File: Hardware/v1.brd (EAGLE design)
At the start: 50 x 40 mm, 79 parts, among them IC1 LM324D, IC2 m328p, IC3 REG1117, J1 22-27-2061-06, J2 22-27-2021-02, J3 22-27-2021-02, J4 22-27-2031-03, J5 22-27-2041-04, Q1 BSS123, Q2 BSS123, Q3 BSS123, Q5 BSS123

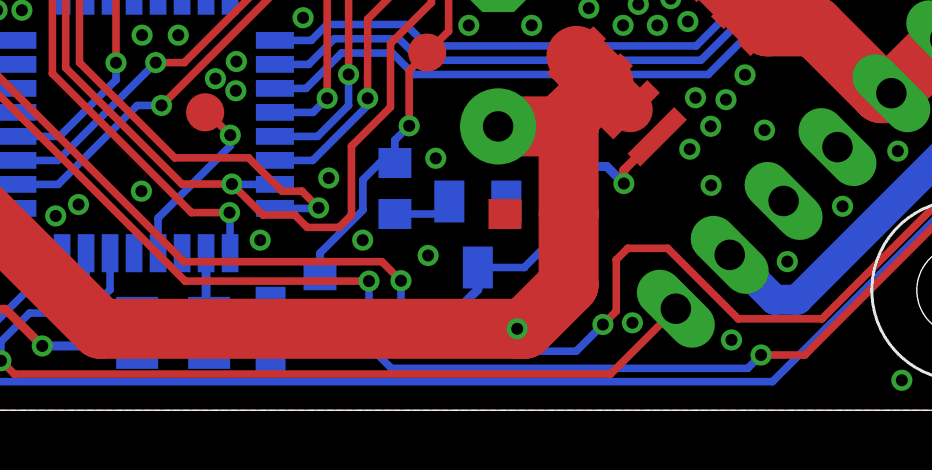
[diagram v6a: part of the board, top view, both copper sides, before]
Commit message: some ground issues fixed
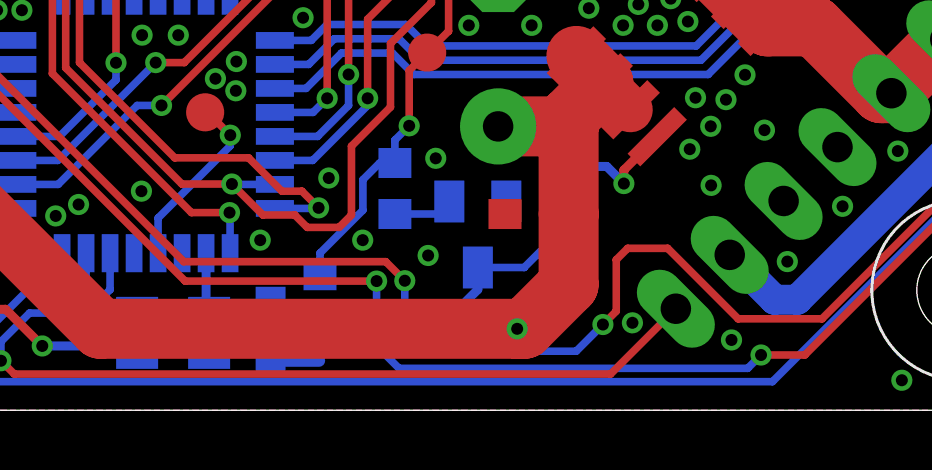
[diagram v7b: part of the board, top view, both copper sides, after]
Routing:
- net GND: track 7.48 -> 9.18 mm
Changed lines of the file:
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@@
 <wire x1="22.098" y1="39.116" x2="22.098" y2="38.13175" width="0.3" layer="16"/>
 <wire x1="22.098" y1="38.13175" x2="22.09165" y2="38.1254" width="0.3" layer="16"/>
-<wire x1="24.60625" y1="2.80125" x2="22.958425" y2="1.864625" width="0" layer="19" extent="16-16"/>
-<wire x1="26.02865" y1="5.67055" x2="24.60625" y2="2.80125" width="0" layer="19" extent="16-16"/>
+<wire x1="22.958425" y1="1.864625" x2="23.17205" y2="1.651" width="0.4064" layer="16"/>
+<wire x1="23.17205" y1="1.651" x2="24.5745" y2="1.651" width="0.4064" layer="16"/>
 </signal>
 <signal name="N$1">
@@
 <wire x1="48.26" y1="12.192" x2="48.26" y2="9.3345" width="0.254" layer="1"/>
 <wire x1="48.26" y1="9.3345" x2="40.767" y2="1.8415" width="0.254" layer="1"/>
-<wire x1="38.862" y1="1.397" x2="26.9875" y2="1.397" width="0.254" layer="16"/>
-<wire x1="26.9875" y1="1.397" x2="26.2382" y2="2.1463" width="0.254" layer="16"/>
-<via x="26.2382" y="4.3053" extent="1-16" drill="0.4"/>
+<wire x1="38.862" y1="1.397" x2="27.2415" y2="1.397" width="0.254" layer="16"/>
+<wire x1="27.2415" y1="1.397" x2="26.4922" y2="2.1463" width="0.254" layer="16"/>
+<via x="26.4922" y="4.3053" extent="1-16" drill="0.4"/>
 <wire x1="38.862" y1="1.397" x2="39.3065" y2="1.8415" width="0.254" layer="16"/>
 <via x="39.3065" y="1.8415" extent="1-16" drill="0.4"/>
-<wire x1="26.2382" y1="4.3053" x2="20.11045" y2="4.3053" width="0.254" layer="1"/>
+<wire x1="26.4922" y1="4.3053" x2="20.11045" y2="4.3053" width="0.254" layer="1"/>
 <wire x1="20.11045" y1="4.3053" x2="12.5095" y2="11.90625" width="0.254" layer="1"/>
 <wire x1="12.5095" y1="11.90625" x2="12.09675" y2="11.90625" width="0.254" layer="1"/>
 <wire x1="39.3065" y1="1.8415" x2="40.767" y2="1.8415" width="0.254" layer="1"/>
-<wire x1="26.2382" y1="2.1463" x2="26.2382" y2="4.3053" width="0.254" layer="16"/>
+<wire x1="26.4922" y1="2.1463" x2="26.4922" y2="4.3053" width="0.254" layer="16"/>
 </signal>
 <signal name="BUTTON_-">
@@
 <wire x1="34.8615" y1="5.3975" x2="34.4805" y2="5.0165" width="0.254" layer="1"/>
 <wire x1="34.4805" y1="5.0165" x2="34.4805" y2="3.302" width="0.254" layer="1"/>
-<via x="27.305" y="4.318" extent="1-16" drill="0.4"/>
-<wire x1="27.305" y1="4.318" x2="27.305" y2="2.413" width="0.254" layer="16"/>
-<wire x1="27.305" y1="2.413" x2="27.7495" y2="1.9685" width="0.254" layer="16"/>
-<wire x1="27.7495" y1="1.9685" x2="33.147" y2="1.9685" width="0.254" layer="16"/>
+<via x="27.432" y="4.318" extent="1-16" drill="0.4"/>
+<wire x1="27.432" y1="4.318" x2="27.432" y2="2.413" width="0.254" layer="16"/>
+<wire x1="27.432" y1="2.413" x2="27.8765" y2="1.9685" width="0.254" layer="16"/>
+<wire x1="27.8765" y1="1.9685" x2="33.147" y2="1.9685" width="0.254" layer="16"/>
 <wire x1="33.147" y1="1.9685" x2="34.036" y2="2.8575" width="0.254" layer="16"/>
 <via x="34.036" y="2.8575" extent="1-16" drill="0.4"/>
 <wire x1="34.036" y1="2.8575" x2="34.4805" y2="3.302" width="0.254" layer="1"/>
-<wire x1="27.305" y1="4.318" x2="26.67" y2="4.953" width="0.254" layer="1"/>
-<wire x1="26.67" y1="4.953" x2="20.066" y2="4.953" width="0.254" layer="1"/>
+<wire x1="27.432" y1="4.318" x2="26.797" y2="4.953" width="0.254" layer="1"/>
+<wire x1="26.797" y1="4.953" x2="20.066" y2="4.953" width="0.254" layer="1"/>
 <wire x1="20.066" y1="4.953" x2="12.620625" y2="12.398375" width="0.254" layer="1"/>
 <wire x1="12.620625" y1="12.398375" x2="12.620625" y2="12.85875" width="0.254" layer="1"/>
